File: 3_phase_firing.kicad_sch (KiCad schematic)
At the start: 61 parts, among them J1 IN1, J2 IN2, J3 OUT, Q1 MMBT3904, Q2 MMBT3904, Q3 MMBT3904, Q4 MMBT3904, Q5 MMBT3904, Q6 MMBT3904, U1 LM339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

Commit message: fixing schematics and pcb layout, adding usb and knob control
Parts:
- added J4: USB_B, Connector_USB:USB_B_OST_USB-B1HSxx_Horizontal, symbol Connector:USB_B
- added J5, J7: Conn_01x03, Connector_JST:JST_XH_B3B-XH-A_1x03_P2.50mm_Vertical, symbol Connector_Generic:Conn_01x03
- added J6, J8: Conn_01x02, Connector_JST:JST_XH_B2B-XH-A_1x02_P2.50mm_Vertical, symbol Connector_Generic:Conn_01x02
- D1: symbol Device:D_Bridge_-A+A -> Device:D_Bridge_+-AA
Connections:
- net +3.3V: now also J5.1 (Pin_1), J7.1 (Pin_1)
- net GATE_A1: no longer U6.27 (PA1)
- net GATE_A2: now also U6.7 (PA10); no longer U6.28 (PA2)
- net GATE_B1: now also U6.33 (PA7)
- net GATE_B2: now also U6.34 (PB0)
- net GATE_C1: now also U6.15 (PB7)
- net GATE_C2: now also U6.16 (PB8)
- net GND: now also J5.3 (Pin_3), J6.2 (Pin_2), J7.3 (Pin_3), J8.2 (Pin_2)
- net GNDS: now also D1.2 (-); no longer D1.1 (-)
- net NEUT: now also D1.3; no longer D1.4
- net PHASE_A: now also D1.4; no longer D1.2
- net TRIAC_MODE: now also U6.3 (PB14), J6.1 (Pin_1)
- net ZCD_A: now also U6.31 (PA5); no longer U6.26 (PA0)
- net ZCD_B: now also U6.32 (PA6)
- net ZCD_C: now also U6.14 (PB6)
- net LED_INDICATOR_2: now reaches U6.2 (PB13)
- net LED_INDICATOR_1: now reaches U6.22 (PC13)
- net LED_INDICATOR_1: now also J7.2 (Pin_2)
- net SCR_MODE: now reaches U6.4 (PB15)
- net SCR_MODE: now also J8.1 (Pin_1)
- net DB_D_OUT: now reaches C1.1, D5.1 (K), U2.1 (IN)
- net DB_OUT: now reaches D5.2 (A)
- net DB_OUT: now also D1.1 (+); no longer D1.3 (+)
- new net ANGLE_CONTROL: J5.2 (Pin_2), U6.26 (PA0)
- no-connect marks 0 -> 3
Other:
- note added: "MCU Control"
- note removed: "MCU"
- moved on the sheet: D10, D11, D6, D7, D8, D9, J3, Q1, Q2, Q3, Q4, Q5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

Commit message: done with all revision
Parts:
- removed D11: 1N4007, Diode_SMD:D_SMA_Handsoldering, symbol Device:D
- removed Q1, Q4, Q5, Q6: MMBT3904, Package_TO_SOT_SMD:SOT-23, symbol Device:Q_NPN_BCE
- removed U10, U11, U12, U7, U8, U9: 4N35, Package_DIP:DIP-6_W8.89mm_SMDSocket_LongPads, symbol Isolator:4N35
- added Q2: MMBT3904, Package_TO_SOT_SMD:SOT-23, symbol Device:Q_NPN_BCE
- added Q4, Q5, Q6, Q7, Q8, Q9: TIC106, Package_TO_SOT_THT:TO-220-3_Vertical, symbol Triac_Thyristor:TIC106
- added R28, R29, R30, R31, R32, R33, R34, R35, R36, R37, R38, R39: 1K, Resistor_SMD:R_1206_3216Metric_Pad1.30x1.75mm_HandSolder, symbol Device:R
- added R40: 220, Resistor_SMD:R_1206_3216Metric_Pad1.30x1.75mm_HandSolder, symbol Device:R
- added R41, R42: 10K, Resistor_SMD:R_0805_2012Metric, symbol Device:R
- added U10, U11, U12, U7, U8, U9: MOC3021M, Package_DIP:DIP-6_W8.89mm_SMDSocket_LongPads, symbol Relay_SolidState:MOC3021M
- J3: value OUT -> OUTPUT; footprint TerminalBlock_Phoenix:TerminalBlock_Phoenix_MKDS-3-12-5.08_1x12_P5.08mm_Horizontal -> TerminalBlock_Phoenix:TerminalBlock_Phoenix_MKDS-1,5-12-5.08_1x12_P5.08mm_Horizontal
- J5: value Conn_01x03 -> KNOB_ANGLE
- J6: value Conn_01x02 -> TRIAC_BUTTON_CONN
- J7: value Conn_01x03 -> LED_CONN
- J8: value Conn_01x02 -> SCR_BUTTON_CONN
- R22, R23, R24, R25, R26, R27: value 2K2 -> 220
- U6: value YAAJ_WeAct_BlackPill_Part_Like -> STM32F401CCU6
- renumbered Q2 to Q1
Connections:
- net OUTA2_E is gone; now on net A: J3.9 (Pin_9)
- net +3.3V: now also R41.2, R42.2
- net DB_D_OUT: now also D1.1 (+); no longer D5.1 (K)
- net GATE_A1: now also Q1.3 (E), R24.2; no longer D8.2 (A)
- net GATE_A2: now also Q1.2 (C), R23.2, U6.37 (PB10); no longer D9.2 (A), U6.7 (PA10)
- net GATE_B1: now also R22.2, Q2.3 (E); no longer D6.2 (A)
- net GATE_B2: now also R25.2, Q2.2 (C); no longer D7.2 (A)
- net GATE_C1: now also Q3.3 (E), R26.2; no longer D10.2 (A)
- net GATE_C2: now also Q3.2 (C), R27.2
- net GND: now also J4.4 (GND), U10.2, U11.2, U12.2, U7.2, U8.2, U9.2
- net LED_INDICATOR_1: now also R40.2; no longer J7.2 (Pin_2)
- net SCR_MODE: now also R42.1
- net TRIAC_MODE: now also R41.1; no longer Q1.1 (B), Q3.1 (B)
- net +5V: now reaches U6.40 (5V)
- net +5V: now also J4.1 (VBUS)
- net USB+: now reaches U6.8 (PA11)
- net USB+: now also J4.3 (D+)
- net USB-: now reaches U6.9 (PA12)
- net USB-: now also J4.2 (D-)
- net at D7.1 (K): now also U11.6; no longer R23.2
- net at R24.1: now also U7.1
- net at R25.1: now also U10.1
- net at R22.1: now also U9.1
- net at R26.1: now also U11.1
- net at R27.1: now also U12.1
- net at R23.1: now also U8.1
- net at D6.1 (K): now also U9.6; no longer R22.2
- net DB_OUT renamed A
- net A: now also Q4.2 (A), Q5.1 (K); no longer D1.1 (+)
- net OUTA1_C renamed LOAD_A
- net LOAD_A: now also D8.2 (A), Q4.1 (K), Q5.2 (A)
- net OUTA1_E renamed SCR_G1_A
- net SCR_G1_A: now also Q4.3 (G), R28.1, R29.1
- net OUTA2_C renamed SCR_G2_A
- net SCR_G2_A: now also Q5.3 (G), R30.1, R31.1
- net OUTB1_C renamed LOAD_B
- net LOAD_B: now also D9.2 (A), Q6.1 (K), Q7.2 (A)
- net OUTB1_E renamed SCR_G1_B
- net SCR_G1_B: now also Q6.3 (G), R32.1, R33.1
- net OUTB2_C renamed SCR_G2_B
- net SCR_G2_B: now also Q7.3 (G), R34.1, R35.1
- net OUTB2_E renamed B
- net B: now also D6.2 (A), Q6.2 (A), Q7.1 (K)
- net OUTC1_C renamed LOAD_C
- net LOAD_C: now also D10.2 (A), Q8.1 (K), Q9.2 (A)
- net OUTC1_E renamed SCR_G1_C
- net SCR_G1_C: now also Q8.3 (G), R36.1, R37.1
- net OUTC2_C renamed SCR_G2_C
- net SCR_G2_C: now also Q9.3 (G), R38.1, R39.1
- net OUTC2_E renamed C
- net C: now also D7.2 (A), Q8.2 (A), Q9.1 (K)
- new net: J7.2 (Pin_2), R40.1
- new net: R28.2, R29.2, U7.4
- new net: D5.1 (K), U7.6
- new net: D9.1 (K), U10.4
- new net: R34.2, R35.2, U10.6
- new net: R32.2, R33.2, U9.4
- new net: R36.2, R37.2, U11.4
- new net: R38.2, R39.2, U12.6
- new net: R30.2, R31.2, U8.6
- new net: D10.1 (K), U12.4
- new net: D8.1 (K), U8.4
- new net MODE_SELECT: Q1.1 (B), Q2.1 (B), Q3.1 (B), U6.7 (PA10)
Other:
- moved on the sheet: C1, C2, J4, J5, J6, J7, J8, Q1, R24, U1E, U2, U6

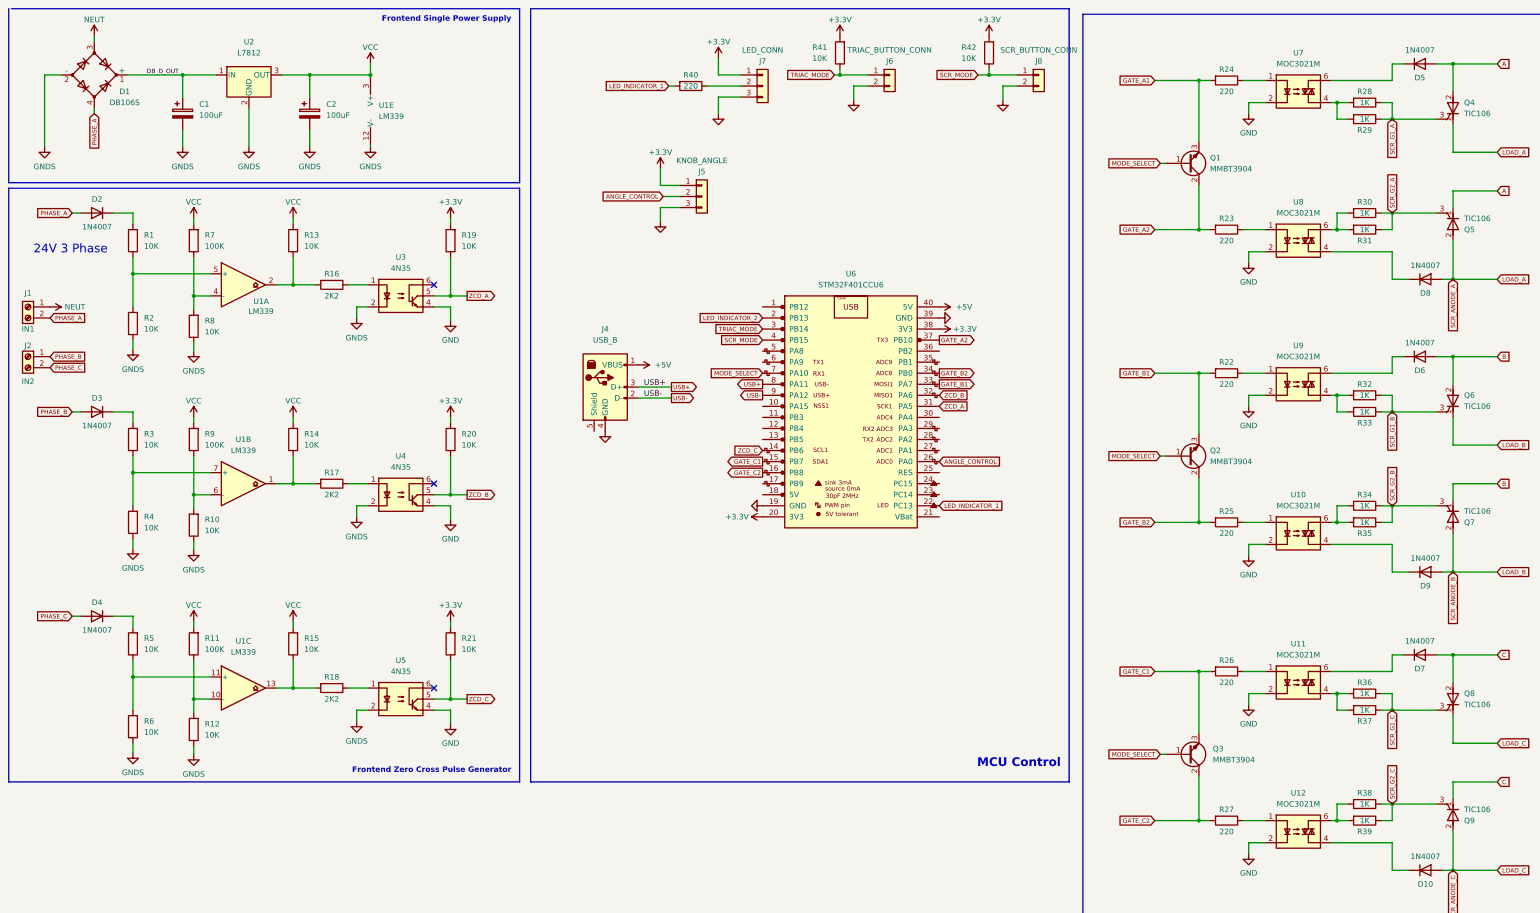
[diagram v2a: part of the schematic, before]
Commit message: fixing psu issue and 3d libs update
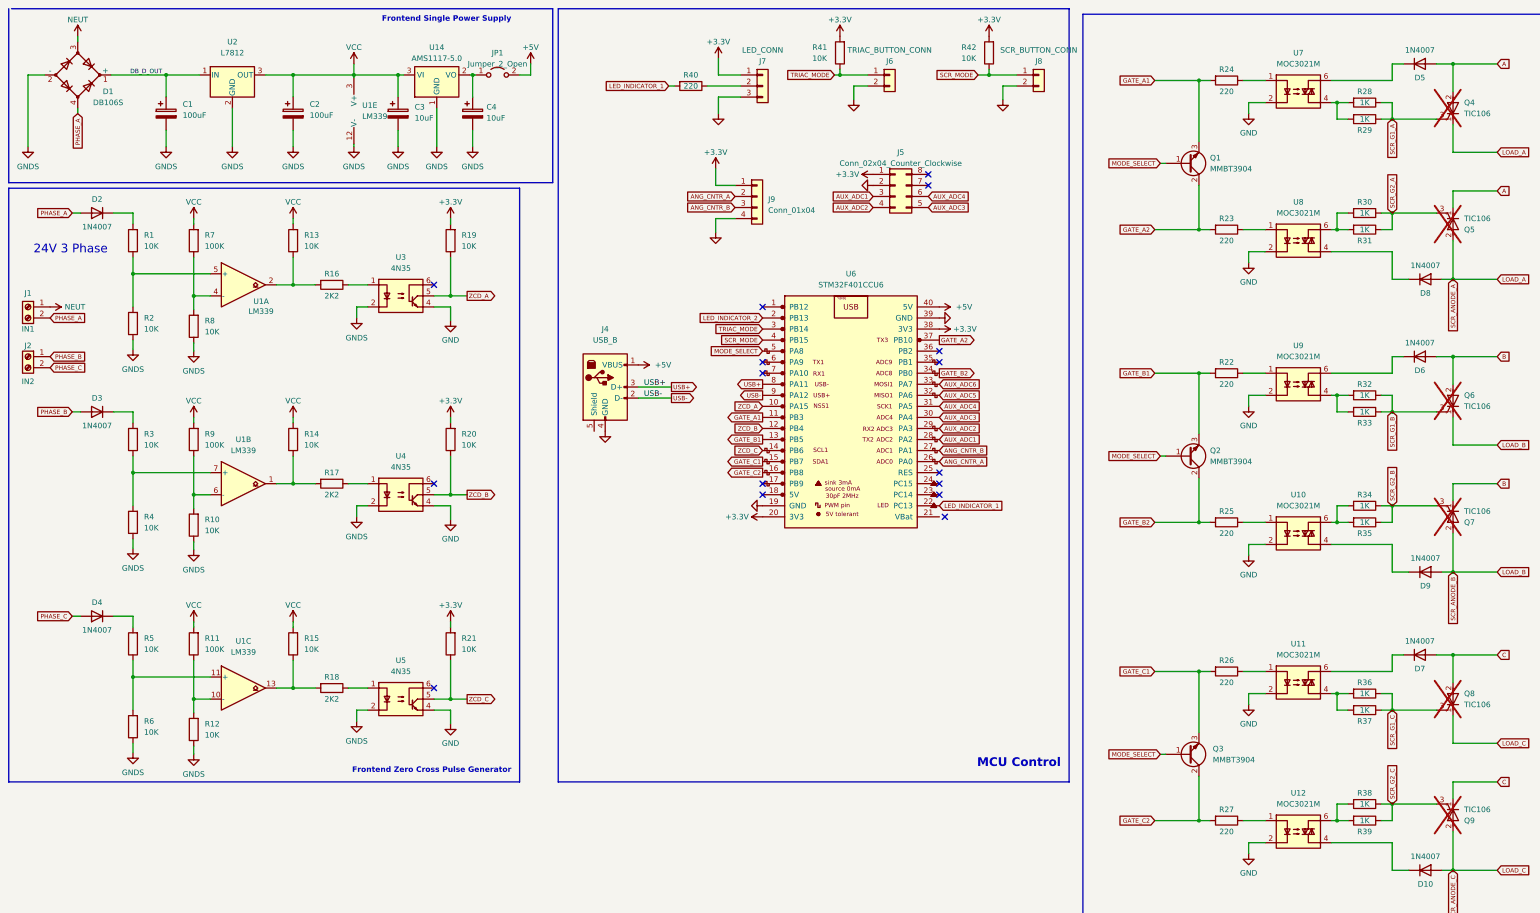
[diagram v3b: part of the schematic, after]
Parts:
- removed J5: KNOB_ANGLE, Connector_JST:JST_XH_B3B-XH-A_1x03_P2.50mm_Vertical, symbol Connector_Generic:Conn_01x03
- added C3, C4: 10uF, Capacitor_SMD:CP_Elec_6.3x7.7, symbol Device:C_Polarized
- added J5: Conn_02x04_Counter_Clockwise, Connector_PinHeader_2.54mm:PinHeader_2x04_P2.54mm_Vertical, symbol Connector_Generic:Conn_02x04_Counter_Clockwise
- added J9: Conn_01x04, Connector_JST:JST_XH_B4B-XH-A_1x04_P2.50mm_Vertical, symbol Connector_Generic:Conn_01x04
- added JP1: Jumper_2_Open, Connector_PinHeader_2.54mm:PinHeader_1x02_P2.54mm_Vertical, symbol Jumper:Jumper_2_Open
- added U14: AMS1117-5.0, Package_TO_SOT_SMD:SOT-223-3_TabPin2, symbol Regulator_Linear:AMS1117-5.0
- Q4, Q5, Q6, Q7, Q8, Q9: now not fitted
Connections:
- net +3.3V: now also J5.1 (Pin_1), J9.1 (Pin_1)
- net +5V: now also JP1.2 (B)
- net GATE_A1: now also U6.11 (PB3)
- net GATE_B1: now also U6.13 (PB5); no longer U6.33 (PA7)
- net GND: now also J5.2 (Pin_2), J9.4 (Pin_4)
- net GNDS: now also C3.2, C4.2, U14.1 (GND)
- net MODE_SELECT: now also U6.5 (PA8); no longer U6.7 (PA10)
- net VCC: now also C3.1, U14.3 (VI)
- net ZCD_A: now also U6.10 (PA15); no longer U6.31 (PA5)
- net ZCD_B: now also U6.12 (PB4); no longer U6.32 (PA6)
- net ANG_CNTR_B: now reaches U6.27 (PA1)
- net ANG_CNTR_B: now also J9.3 (Pin_3)
- net AUX_ADC1: now reaches U6.28 (PA2)
- net AUX_ADC1: now also J5.3 (Pin_3)
- net AUX_ADC2: now reaches U6.29 (PA3)
- net AUX_ADC2: now also J5.4 (Pin_4)
- net AUX_ADC3: now reaches U6.30 (PA4)
- net AUX_ADC3: now also J5.5 (Pin_5)
- net ANGLE_CONTROL renamed ANG_CNTR_A
- net ANG_CNTR_A: now also J9.2 (Pin_2)
- new net: C4.1, JP1.1 (A), U14.2 (VO)
- new net AUX_ADC4: J5.6 (Pin_6), U6.31 (PA5)
- new net AUX_ADC5: U6.32 (PA6)
- new net AUX_ADC6: U6.33 (PA7)
- no-connect marks 3 -> 16
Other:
- moved on the sheet: C1, C2, D1, U1E, U2

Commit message: fixing unconnected bootstrap
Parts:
- removed D10, D5, D6, D7, D8, D9: 1N4007, Diode_SMD:D_SMA_Handsoldering, symbol Device:D
- removed J3: OUTPUT, TerminalBlock_Phoenix:TerminalBlock_Phoenix_MKDS-1,5-12-5.08_1x12_P5.08mm_Horizontal, symbol Connector:Screw_Terminal_01x12
- removed Q4, Q5, Q6, Q7, Q8, Q9: TIC106, Package_TO_SOT_THT:TO-220-3_Vertical, symbol Triac_Thyristor:TIC106
- removed R28, R29, R30, R31, R32, R33, R34, R35, R36, R37, R38, R39: 1K, Resistor_SMD:R_1206_3216Metric_Pad1.30x1.75mm_HandSolder, symbol Device:R
- removed U10, U11, U12, U7, U8, U9: MOC3021M, Package_DIP:DIP-6_W8.89mm_SMDSocket_LongPads, symbol Relay_SolidState:MOC3021M
- added J10: Conn_01x08, Connector_JST:JST_XH_B8B-XH-A_1x08_P2.50mm_Vertical, symbol Connector_Generic:Conn_01x08
- added JP2: Jumper_2_Open, Connector_PinHeader_2.54mm:PinHeader_1x02_P2.54mm_Vertical, symbol Jumper:Jumper_2_Open
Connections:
- net +3.3V: now also J10.1 (Pin_1)
- net GND: now also J10.8 (Pin_8), JP2.2 (B)
- net GNDS: now also JP2.1 (A)
- net at R26.1: now also J10.6 (Pin_6)
- net at R24.1: now also J10.2 (Pin_2)
- net at R25.1: now also J10.5 (Pin_5)
- net at R27.1: now also J10.7 (Pin_7)
- net at R22.1: now also J10.4 (Pin_4)
- net at R23.1: now also J10.3 (Pin_3)
